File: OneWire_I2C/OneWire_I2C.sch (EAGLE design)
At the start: 11 parts, among them M1 BSS84

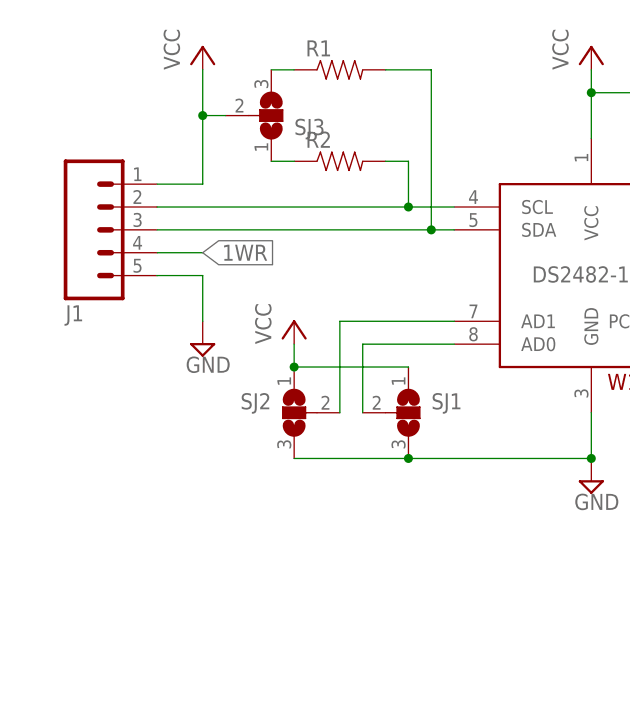
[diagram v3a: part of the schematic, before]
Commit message: Added extra screw terminals on I2C side
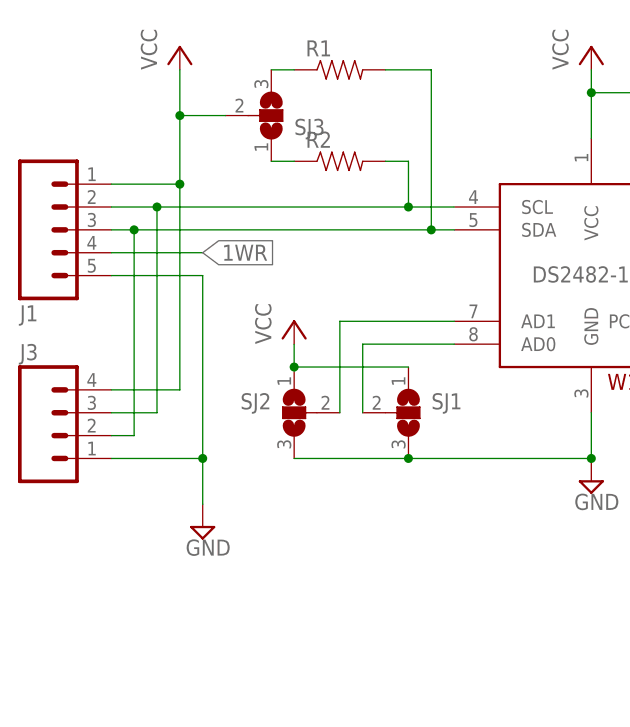
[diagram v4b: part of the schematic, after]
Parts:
- added J3: (no value), SparkFun-Connectors:M04SCREW
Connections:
- net GND: now also J3.1
- net SCL: now also J3.3
- net SDA: now also J3.2
- net VCC: now also J3.4
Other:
- moved on the sheet: J1
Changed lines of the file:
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@@
 <part name="M1" library="Puffin" deviceset="BSS84" device=""/>
 <part name="SJ3" library="jumper" deviceset="SJ2W" device=""/>
+<part name="J3" library="SparkFun-Connectors" deviceset="M04" device="SCREW"/>
 </parts>
 <sheets>
@@
 <instances>
 <instance part="SUPPLY3" gate="GND" x="119.38" y="53.34"/>
-<instance part="SUPPLY4" gate="GND" x="30.48" y="53.34"/>
+<instance part="SUPPLY4" gate="GND" x="30.48" y="33.02"/>
 <instance part="P+1" gate="VCC" x="73.66" y="86.36"/>
-<instance part="P+3" gate="VCC" x="30.48" y="86.36"/>
+<instance part="P+3" gate="VCC" x="27.94" y="86.36"/>
 <instance part="C1" gate="G$1" x="88.9" y="76.2"/>
 <instance part="R1" gate="G$1" x="45.72" y="83.82"/>
@@
 <instance part="P+4" gate="VCC" x="40.64" y="55.88"/>
 <instance part="R3" gate="G$1" x="106.68" y="76.2" rot="R90"/>
-<instance part="J1" gate="G$1" x="17.78" y="66.04" rot="MR180"/>
+<instance part="J1" gate="G$1" x="12.7" y="66.04" rot="MR180"/>
 <instance part="FRAME1" gate="G$1" x="-45.72" y="-40.64"/>
 <instance part="FRAME1" gate="G$2" x="101.6" y="-40.64"/>
@@
 <instance part="M1" gate="G$1" x="99.06" y="55.88"/>
 <instance part="SJ3" gate="G$1" x="38.1" y="78.74" rot="MR180"/>
+<instance part="J3" gate="G$1" x="15.24" y="43.18"/>
 </instances>
 <busses>
@@
 <segment>
 <pinref part="P+3" gate="VCC" pin="VCC"/>
-<wire x1="30.48" y1="71.12" x2="30.48" y2="78.74" width="0.1524" layer="91"/>
+<wire x1="27.94" y1="71.12" x2="27.94" y2="78.74" width="0.1524" layer="91"/>
 <pinref part="J1" gate="G$1" pin="1"/>
-<wire x1="30.48" y1="78.74" x2="30.48" y2="83.82" width="0.1524" layer="91"/>
-<wire x1="25.4" y1="71.12" x2="30.48" y2="71.12" width="0.1524" layer="91"/>
+<wire x1="27.94" y1="78.74" x2="27.94" y2="83.82" width="0.1524" layer="91"/>
+<wire x1="20.32" y1="71.12" x2="27.94" y2="71.12" width="0.1524" layer="91"/>
 <pinref part="SJ3" gate="G$1" pin="2"/>
-<wire x1="33.02" y1="78.74" x2="30.48" y2="78.74" width="0.1524" layer="91"/>
-<junction x="30.48" y="78.74"/>
+<wire x1="33.02" y1="78.74" x2="27.94" y2="78.74" width="0.1524" layer="91"/>
+<junction x="27.94" y="78.74"/>
+<pinref part="J3" gate="G$1" pin="4"/>
+<wire x1="20.32" y1="48.26" x2="27.94" y2="48.26" width="0.1524" layer="91"/>
+<wire x1="27.94" y1="48.26" x2="27.94" y2="71.12" width="0.1524" layer="91"/>
+<junction x="27.94" y="71.12"/>
 </segment>
 <segment>
@@
 <pinref part="SUPPLY4" gate="GND" pin="GND"/>
 <pinref part="J1" gate="G$1" pin="5"/>
-<wire x1="30.48" y1="55.88" x2="30.48" y2="60.96" width="0.1524" layer="91"/>
-<wire x1="30.48" y1="60.96" x2="25.4" y2="60.96" width="0.1524" layer="91"/>
+<wire x1="30.48" y1="35.56" x2="30.48" y2="40.64" width="0.1524" layer="91"/>
+<wire x1="30.48" y1="40.64" x2="30.48" y2="60.96" width="0.1524" layer="91"/>
+<wire x1="30.48" y1="60.96" x2="20.32" y2="60.96" width="0.1524" layer="91"/>
+<pinref part="J3" gate="G$1" pin="1"/>
+<wire x1="20.32" y1="40.64" x2="30.48" y2="40.64" width="0.1524" layer="91"/>
+<junction x="30.48" y="40.64"/>
 </segment>
 <segment>
@@
 <pinref part="R2" gate="G$1" pin="2"/>
 <wire x1="53.34" y1="68.58" x2="25.4" y2="68.58" width="0.1524" layer="91"/>
+<wire x1="25.4" y1="68.58" x2="20.32" y2="68.58" width="0.1524" layer="91"/>
 <wire x1="50.8" y1="73.66" x2="53.34" y2="73.66" width="0.1524" layer="91"/>
 <wire x1="53.34" y1="73.66" x2="53.34" y2="68.58" width="0.1524" layer="91"/>
 <junction x="53.34" y="68.58"/>
+<pinref part="J3" gate="G$1" pin="3"/>
+<wire x1="20.32" y1="45.72" x2="25.4" y2="45.72" width="0.1524" layer="91"/>
+<wire x1="25.4" y1="45.72" x2="25.4" y2="68.58" width="0.1524" layer="91"/>
+<junction x="25.4" y="68.58"/>
 </segment>
 </net>
@@
 <wire x1="58.42" y1="66.04" x2="55.88" y2="66.04" width="0.1524" layer="91"/>
 <pinref part="R1" gate="G$1" pin="2"/>
-<wire x1="55.88" y1="66.04" x2="25.4" y2="66.04" width="0.1524" layer="91"/>
+<wire x1="55.88" y1="66.04" x2="22.86" y2="66.04" width="0.1524" layer="91"/>
+<wire x1="22.86" y1="66.04" x2="20.32" y2="66.04" width="0.1524" layer="91"/>
 <wire x1="50.8" y1="83.82" x2="55.88" y2="83.82" width="0.1524" layer="91"/>
 <wire x1="55.88" y1="83.82" x2="55.88" y2="66.04" width="0.1524" layer="91"/>
 <junction x="55.88" y="66.04"/>
+<pinref part="J3" gate="G$1" pin="2"/>
+<wire x1="20.32" y1="43.18" x2="22.86" y2="43.18" width="0.1524" layer="91"/>
+<wire x1="22.86" y1="43.18" x2="22.86" y2="66.04" width="0.1524" layer="91"/>
+<junction x="22.86" y="66.04"/>
 </segment>
 </net>
@@
 <segment>
 <pinref part="J1" gate="G$1" pin="4"/>
-<wire x1="25.4" y1="63.5" x2="30.48" y2="63.5" width="0.1524" layer="91"/>
+<wire x1="20.32" y1="63.5" x2="30.48" y2="63.5" width="0.1524" layer="91"/>
 <label x="30.48" y="63.5" size="1.778" layer="95" xref="yes"/>
 </segment>
